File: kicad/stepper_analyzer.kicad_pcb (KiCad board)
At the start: 2 copper layers, 102 x 57 mm, 23 parts, among them J1 Connector_Conn_01x04_Male, J2 Connector_Conn_01x04_Male, M1 Motor, Q1 AO3400A, U1 ACS70331EOLCTR-2P5B3, U2 ACS70331EOLCTR-2P5B3, U3 Pico

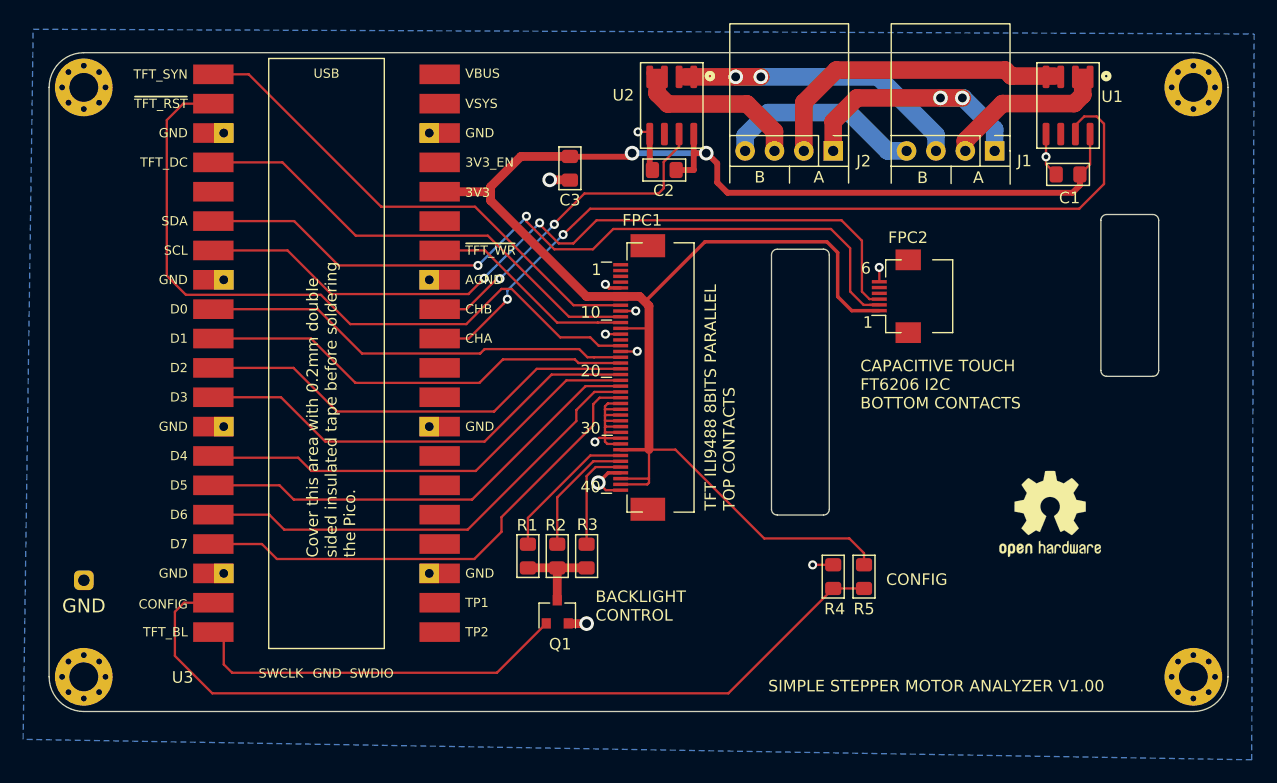
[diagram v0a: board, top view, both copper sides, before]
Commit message: Tweaked silk screen.
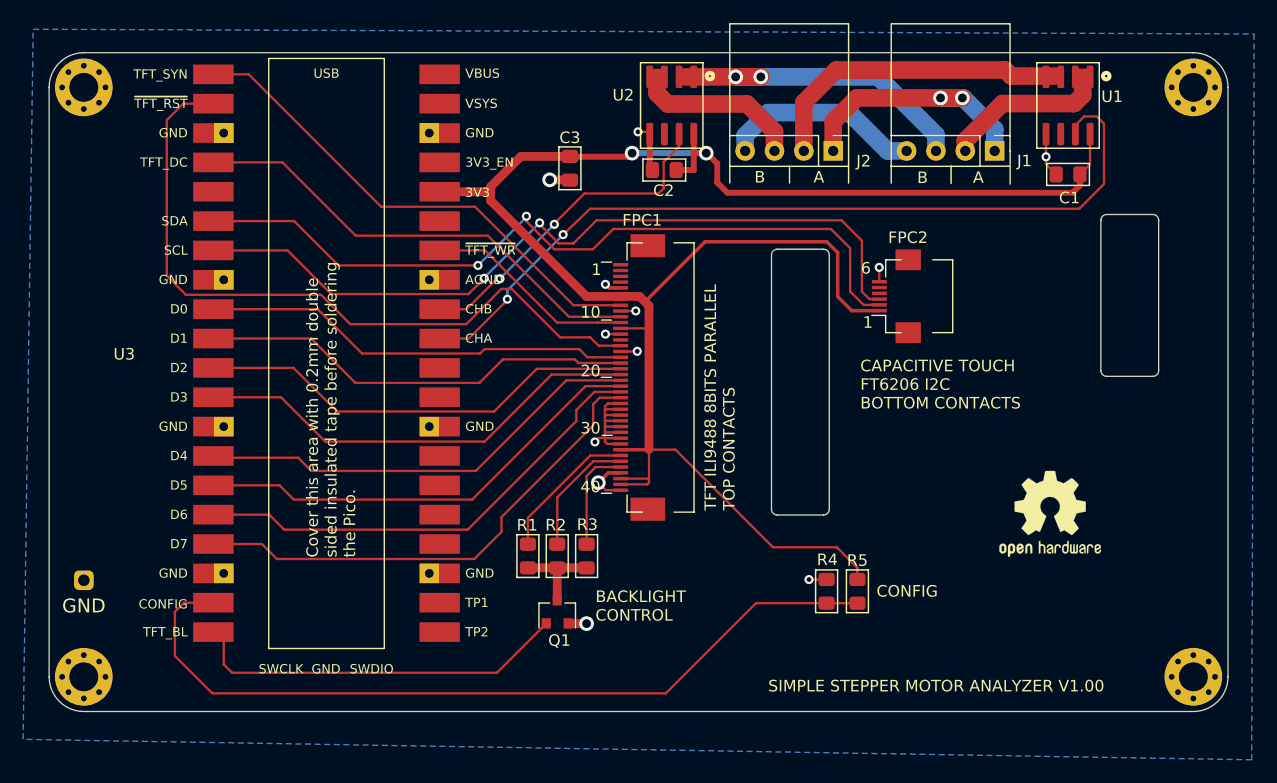
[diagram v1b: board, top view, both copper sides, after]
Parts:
- moved R4 1.39 mm to (66.3, -10.4)
- moved R5 1.39 mm to (68.9, -10.4)
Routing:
- net /CONFIG: track 73.1 -> 72.0 mm

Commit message: Renamed Config to Options
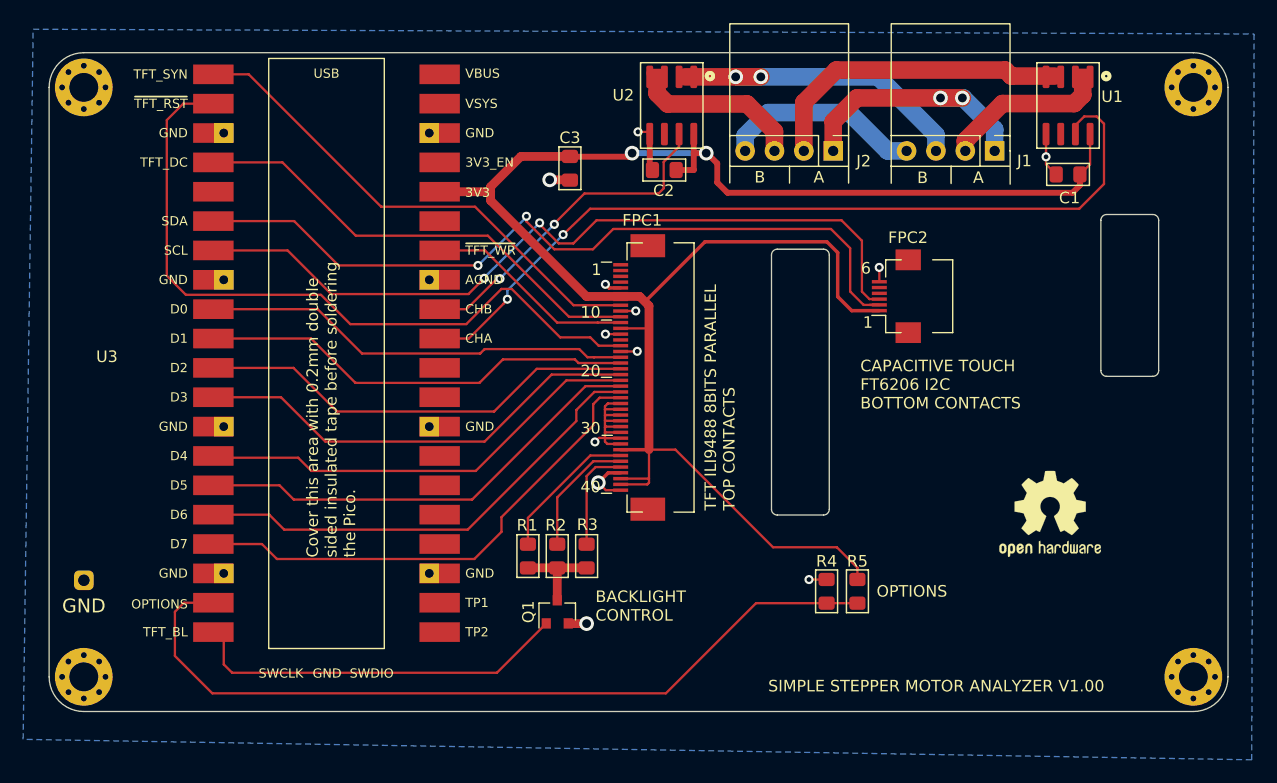
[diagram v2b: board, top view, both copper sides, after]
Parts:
- Q1: footprint stepper_motor_analyzer:SOT-23 -> Package_TO_SOT_SMD:SOT-23
- R4, R5: footprint stepper_motor_analyzer:R_0805_2012Metric_Pad1.15x1.40mm_HandSolder -> stepper_motor_analyzer:R_0805_2012Metric_Pad1.15x1.40mm_HandSolder_no_3d
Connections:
- net /CONFIG renamed /OPTIONS
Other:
- board text added: "OPTIONS"
- board text removed: "CONFIG"

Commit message: Made schematic and PCB changes toward MK3.  Not ready.
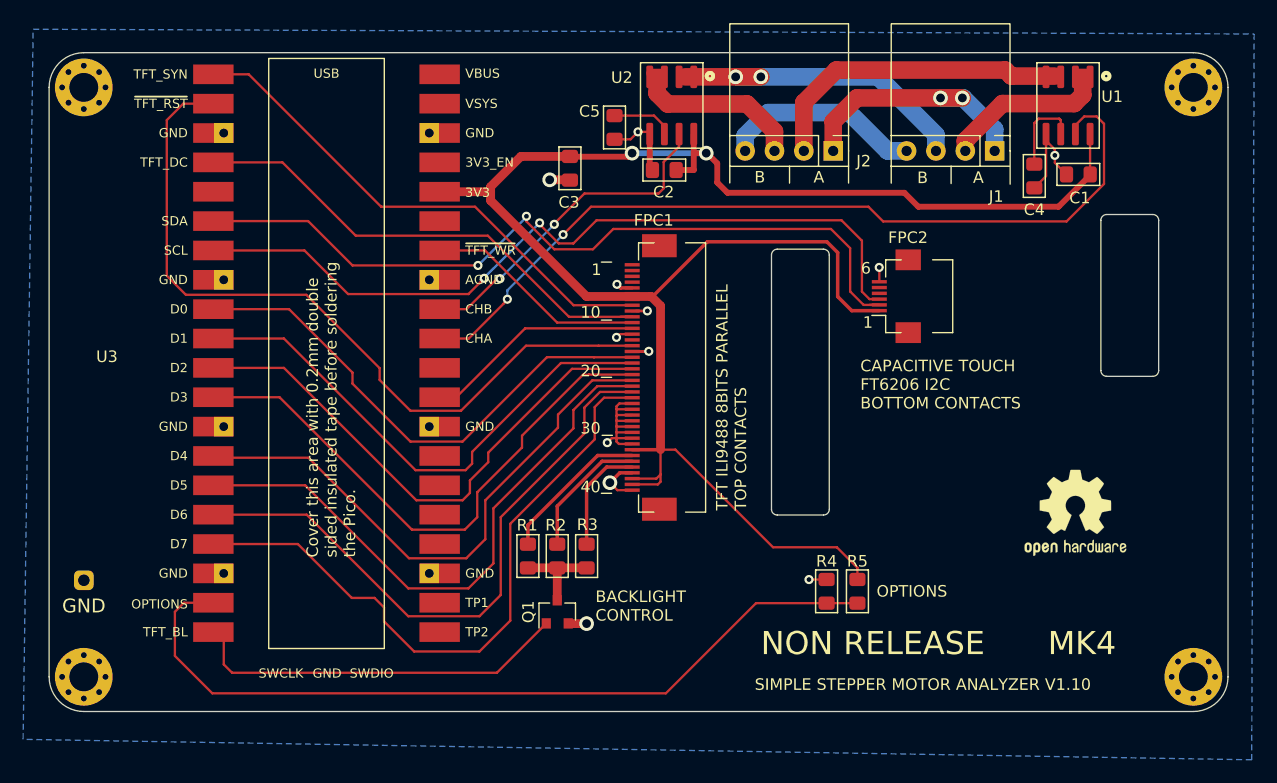
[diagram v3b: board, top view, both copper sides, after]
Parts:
- added C4: DNP, stepper_motor_analyzer:C_0805_2012Metric_Pad1.15x1.40mm_HandSolder, F.Cu at (84.2, -46.3)
- added C5: DNP, stepper_motor_analyzer:C_0805_2012Metric_Pad1.15x1.40mm_HandSolder, F.Cu at (47.9, -50.5)
- moved LOGO1 2.19 mm to (87.8, -17.2)
- moved FPC1 1.00 mm to (51.3, -28.9)
- moved C1 0.89 mm to (88.0, -46.5)
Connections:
- FPC1 pad 12: +3V3 -> /~TFT_RD
- U3 pad 29: Net-(U3-Pad29) -> /~TFT_RD
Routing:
- net /~TFT_RD: track 0.00 -> 20.3 mm
- net /D7: track 42.5 -> 55.6 mm
- net /D6: track 40.4 -> 52.3 mm
- net /D5: track 38.9 -> 50.0 mm
- net /D4: track 38.1 -> 48.0 mm
- net GND: track 39.3 -> 48.6 mm
- net /D3: track 38.3 -> 47.5 mm
- net /D2: track 37.4 -> 45.9 mm
- net /D1: track 36.9 -> 44.5 mm
- net Net-(C4-Pad2): track 0.00 -> 7.47 mm
- net /D0: track 36.4 -> 43.7 mm
- net Net-(C5-Pad2): track 0.00 -> 5.39 mm
- net /~TFT_RST: track 63.3 -> 67.0 mm
- net +3V3: track 165.2 -> 162.9 mm
- net /TFT_DC: track 39.9 -> 41.9 mm
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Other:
- board text added: "MK4"
- board text added: "NON RELEASE"
- board text added: "SIMPLE STEPPER MOTOR ANALYZER V1.10"
- board text removed: "SIMPLE STEPPER MOTOR ANALYZER V1.00"

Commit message: Teaked board design toward MK4.
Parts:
- C4: value DNP -> 1nf
- R4: footprint stepper_motor_analyzer:R_0805_2012Metric_Pad1.15x1.40mm_HandSolder_no_3d -> stepper_motor_analyzer:R_0805_2012Metric_Pad1.15x1.40mm_HandSolder
- U1, U2: value ACS70331EOLCTR-2P5B3 -> (CURRENT SENSOR)
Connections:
- U3 pad 27: Net-(U3-Pad27) -> GND
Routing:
- net GND: track 48.6 -> 53.1 mm, vias 12 -> 13
- net /OPTIONS: track 72.0 -> 72.5 mm

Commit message: Resoted Kicad files to V1.00 release.
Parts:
- removed C4: 1nf, stepper_motor_analyzer:C_0805_2012Metric_Pad1.15x1.40mm_HandSolder
- removed C5: DNP, stepper_motor_analyzer:C_0805_2012Metric_Pad1.15x1.40mm_HandSolder
- R4: footprint stepper_motor_analyzer:R_0805_2012Metric_Pad1.15x1.40mm_HandSolder -> stepper_motor_analyzer:R_0805_2012Metric_Pad1.15x1.40mm_HandSolder_no_3d
- U1, U2: value (CURRENT SENSOR) -> ACS70331EOLCTR-2P5B3
- moved LOGO1 2.19 mm to (85.6, -17.1)
- moved FPC1 1.00 mm to (50.3, -28.9)
- moved C1 0.89 mm to (87.2, -46.5)
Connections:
- FPC1 pad 12: /~TFT_RD -> +3V3
- U3 pad 27: GND -> Net-(U3-Pad27)
- U3 pad 29: /~TFT_RD -> Net-(U3-Pad29)
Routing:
- net /~TFT_RD: track 20.3 -> 0.00 mm
- net GND: track 53.1 -> 39.3 mm, vias 13 -> 12
- net /D7: track 55.6 -> 42.5 mm
- net /D6: track 52.3 -> 40.4 mm
- net /D5: track 50.0 -> 38.9 mm
- net /D4: track 48.0 -> 38.1 mm
- net /D3: track 47.5 -> 38.3 mm
- net /D2: track 45.9 -> 37.4 mm
- net /D1: track 44.5 -> 36.9 mm
- net /D0: track 43.7 -> 36.4 mm
- net Net-(U1-Pad6): track 7.10 -> 0.00 mm
- net Net-(U2-Pad6): track 5.24 -> 0.00 mm
- net /~TFT_RST: track 67.0 -> 63.3 mm
- net +3V3: track 162.7 -> 165.2 mm
- net /TFT_DC: track 41.9 -> 39.9 mm
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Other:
- board text added: "SIMPLE STEPPER MOTOR ANALYZER V1.00"
- board text removed: "MK4"
- board text removed: "NON RELEASE"
- board text removed: "SIMPLE STEPPER MOTOR ANALYZER V1.10"
